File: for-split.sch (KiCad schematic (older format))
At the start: 77 parts, among them J1 TRRS, J2 TRRS, U1 ProMicro

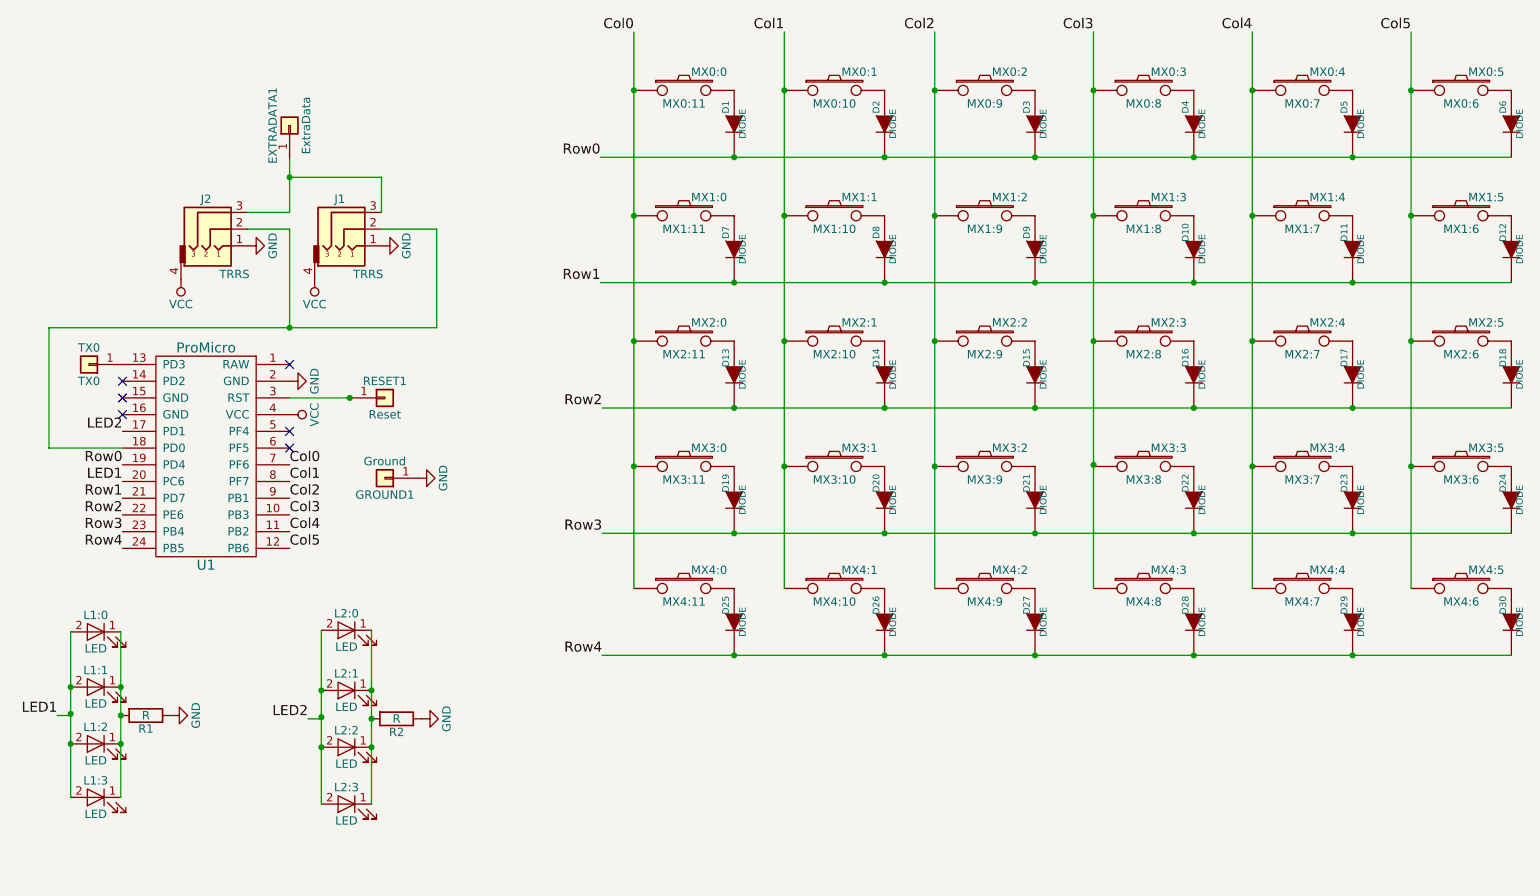
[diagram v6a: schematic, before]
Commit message: Add connectors for rows and columns
Changes have been made to add connectors for the rows and columns so that two PCBs can be bridged together to create a single 12x5 matrix running from a single Pro Micro.
Provision for removal of the bottom row has been removed to make way for the connectors.
Holes for 2U stablizers have been removed to increase PCB stiffness.
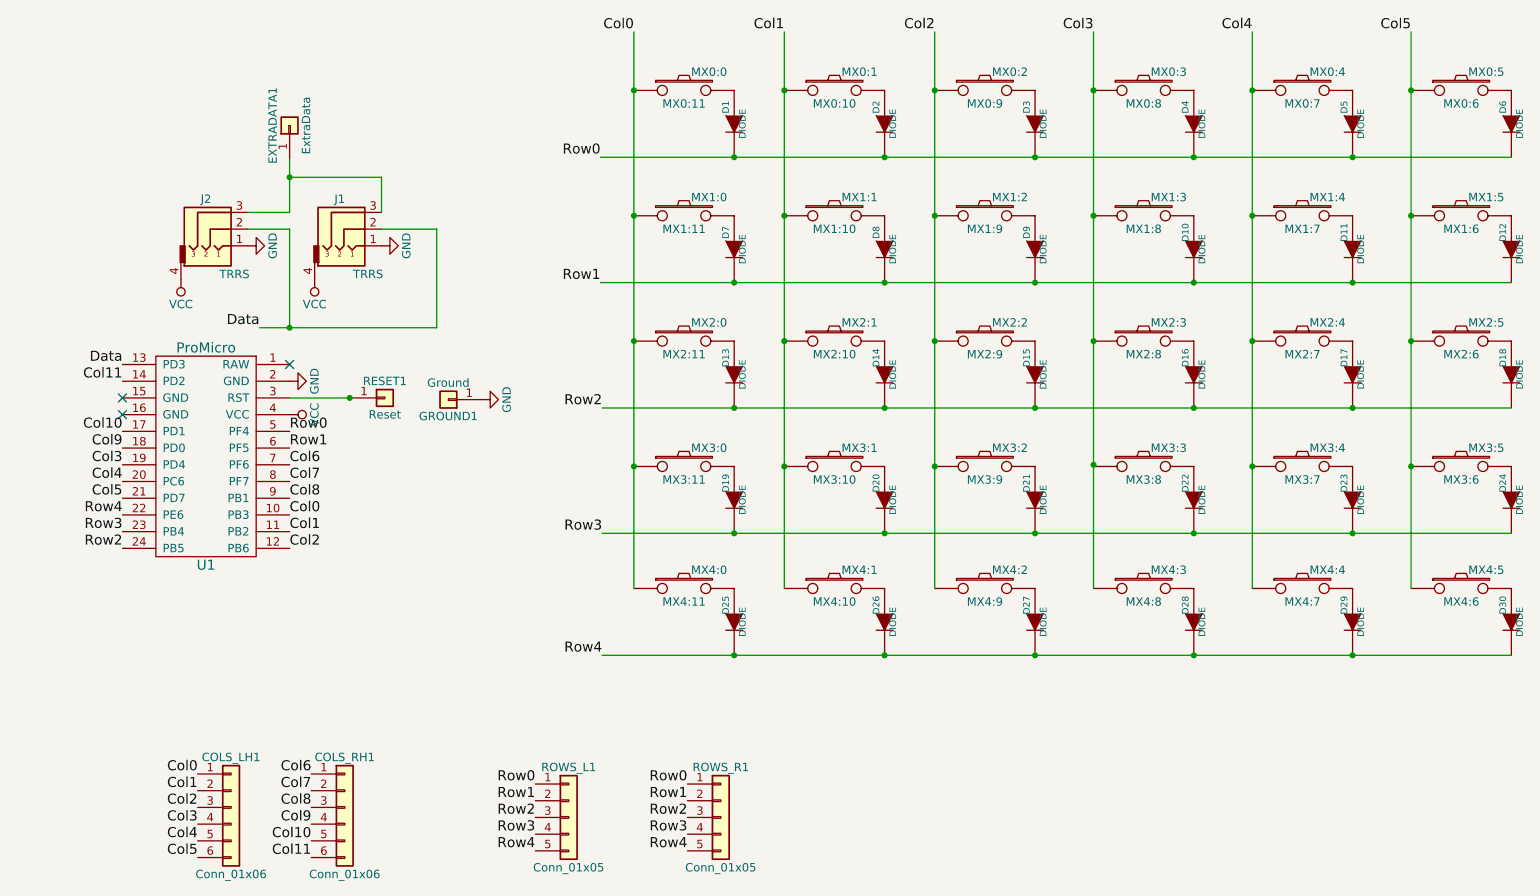
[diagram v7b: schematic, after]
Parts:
- removed L1:0, L1:1, L1:2, L1:3, L2:0, L2:1, L2:2, L2:3: LED, idle-hands:MX_LED, symbol LED
- removed R1, R2: R, Resistors_THT:R_Axial_DIN0207_L6.3mm_D2.5mm_P10.16mm_Horizontal, symbol R
- removed TX0: TX0, canadian_footprints:SIngle_Pad, symbol Conn_01x01
- added COLS_LH1, COLS_RH1: Conn_01x06, idle-hands:CONNECTOR_6, symbol Conn_01x06
- added ROWS_L1, ROWS_R1: Conn_01x05, idle-hands:CONNECTOR_5, symbol Conn_01x05
- EXTRADATA1: footprint canadian_footprints:SIngle_Pad -> idle-hands:Single_Pad
- GROUND1, RESET1: footprint canadian_footprints:SIngle_Pad -> idle-hands:Square_Pad
- J1, J2: footprint Connectors:PJ320D_3.5mm_Jack -> idle-hands:PJ-320A
- MX0:0, MX0:4: footprint idle-hands:MX_CUTOUT_PAD1 -> idle-hands:MX_CUTOUT
- MX0:1, MX0:5: footprint idle-hands:MX_CUTOUT_PAD3 -> idle-hands:MX_CUTOUT
- MX0:2: footprint idle-hands:MX_CUTOUT -> idle-hands:MX_CUTOUT_NTHSTH
- MX4:0, MX4:4: footprint idle-hands:MX -> idle-hands:MX_CUTOUT
- MX4:1, MX4:5: footprint idle-hands:MX2U_CUTOUT -> idle-hands:MX_CUTOUT
- U1: footprint idle-hands:Pro_Micro -> idle-hands:Pro_Micro_ChipSideDown
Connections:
- net LED1 is gone; now on net Col4: U1.20 (PC6)
- net Col0: now also U1.10 (PB3), COLS_LH1.1 (Pin_1); no longer U1.7 (PF6)
- net Col1: now also U1.11 (PB2), COLS_LH1.2 (Pin_2); no longer U1.8 (PF7)
- net Col2: now also U1.12 (PB6), COLS_LH1.3 (Pin_3); no longer U1.9 (PB1)
- net Col3: now also U1.19 (PD4), COLS_LH1.4 (Pin_4); no longer U1.10 (PB3)
- net Col4: now also COLS_LH1.5 (Pin_5); no longer U1.11 (PB2)
- net Col5: now also U1.21 (PD7), COLS_LH1.6 (Pin_6); no longer U1.12 (PB6)
- net Row0: now also U1.5 (PF4), ROWS_L1.1 (Pin_1), ROWS_R1.1 (Pin_1); no longer U1.19 (PD4)
- net Row1: now also U1.6 (PF5), ROWS_L1.2 (Pin_2), ROWS_R1.2 (Pin_2); no longer U1.21 (PD7)
- net Row2: now also U1.24 (PB5), ROWS_L1.3 (Pin_3), ROWS_R1.3 (Pin_3); no longer U1.22 (PE6)
- net Row3: now also ROWS_L1.4 (Pin_4), ROWS_R1.4 (Pin_4)
- net Row4: now also U1.22 (PE6), ROWS_L1.5 (Pin_5), ROWS_R1.5 (Pin_5); no longer U1.24 (PB5)
- net Data: now reaches J1.2, J2.2
- net Data: now also U1.13 (PD3); no longer U1.18 (PD0)
- net Col11: now reaches U1.14 (PD2)
- net Col11: now also COLS_RH1.6 (Pin_6)
- net LED2 renamed Col10
- net Col10: now also COLS_RH1.5 (Pin_5)
- new net Col6: COLS_RH1.1 (Pin_1), U1.7 (PF6)
- new net Col7: COLS_RH1.2 (Pin_2), U1.8 (PF7)
- new net Col8: COLS_RH1.3 (Pin_3), U1.9 (PB1)
- new net Col9: COLS_RH1.4 (Pin_4), U1.18 (PD0)
- no-connect marks 6 -> 3
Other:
- moved on the sheet: GROUND1
